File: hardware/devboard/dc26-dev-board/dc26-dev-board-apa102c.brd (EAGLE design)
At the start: 160 x 100 mm, 84 parts, among them CN1 JST, IC1 STM32F411RET6, M10 STM32-Breakout-2, P1 SSSS811101, U1 ESP-WROOM-32, Y1 ABL-8.000MHZ-B2

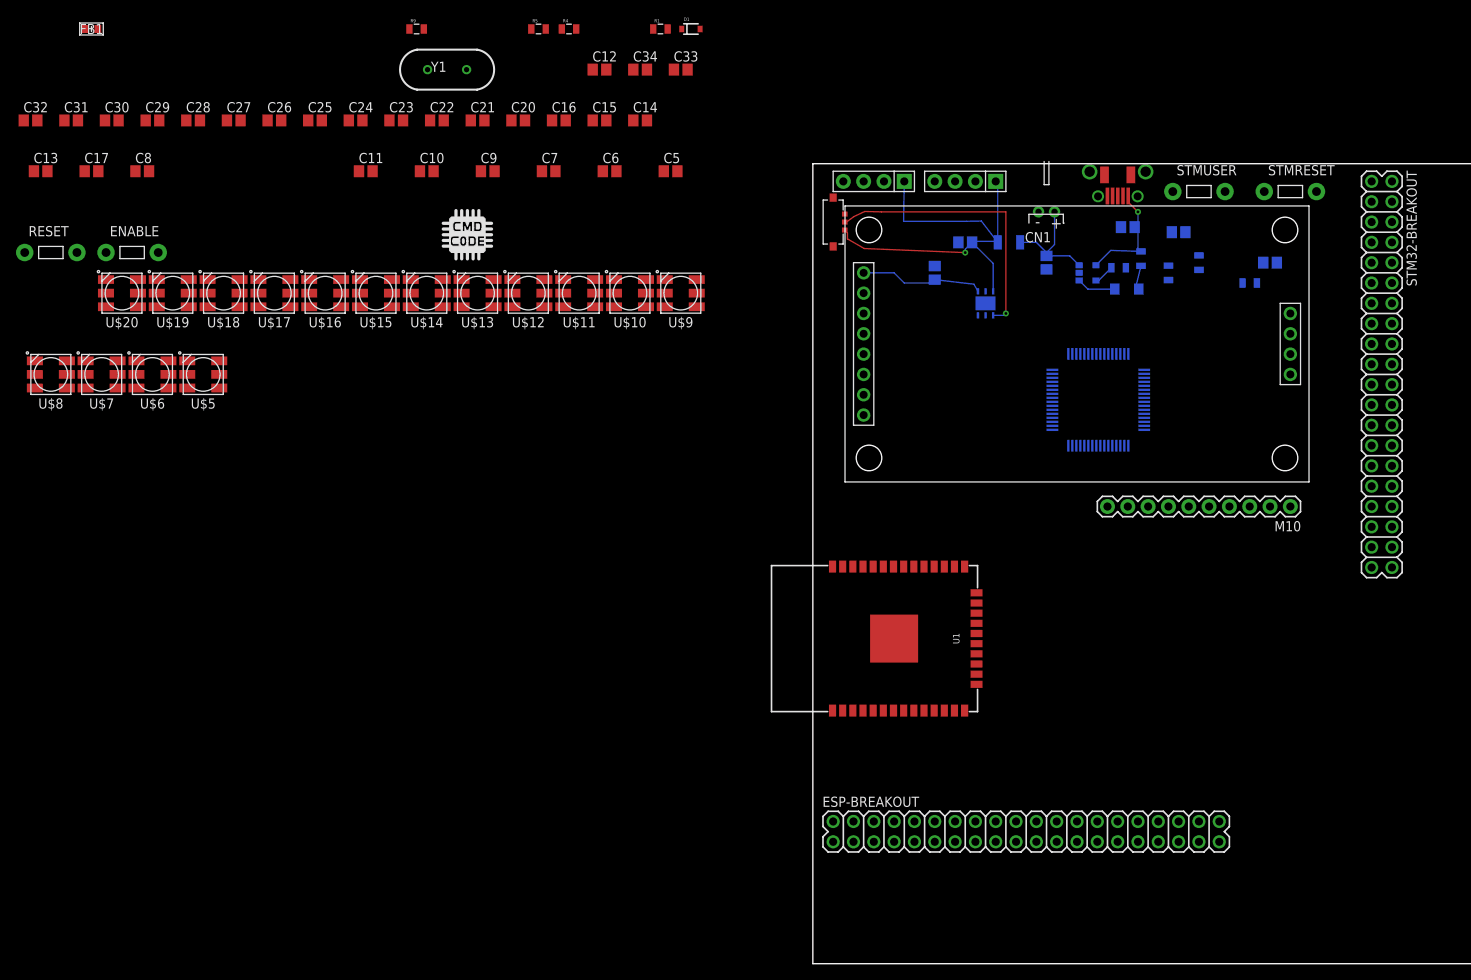
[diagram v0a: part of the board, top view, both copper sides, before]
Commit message: power run not but not gpio
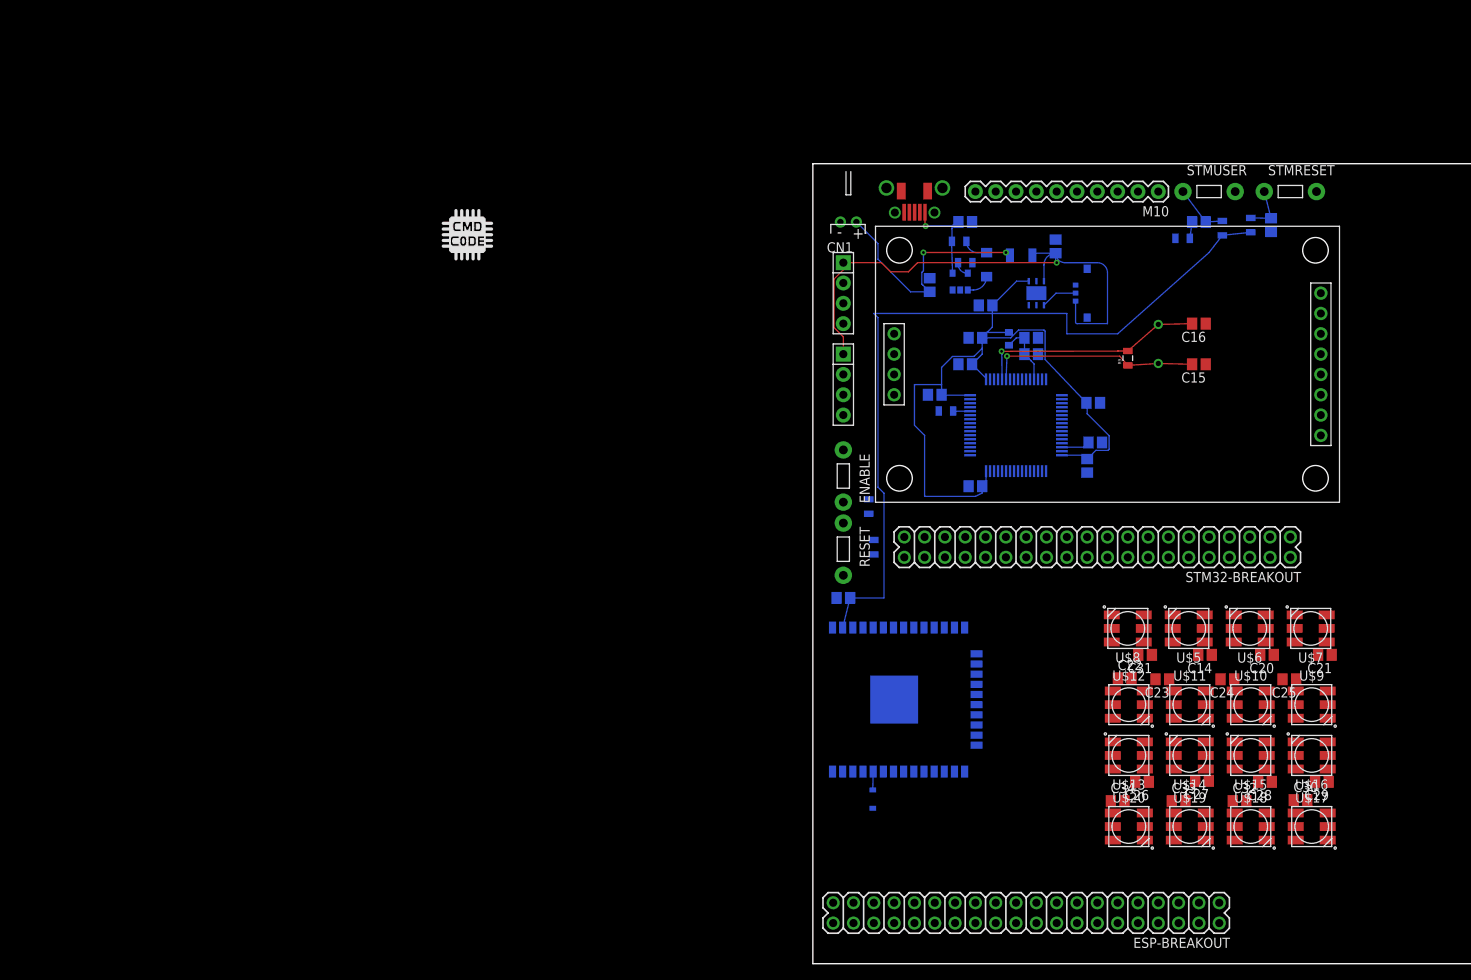
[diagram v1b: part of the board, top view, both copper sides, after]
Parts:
- moved C32 173.4 mm to (53.3, 20.3)
- moved C30 171.2 mm to (61.0, 20.4)
- moved C29 167.9 mm to (63.6, 22.7), turned to 180 degrees
- moved C28 157.4 mm to (56.5, 22.7), turned to 180 degrees
- moved U$7 154.4 mm to (62.2, 41.9)
- moved C31 149.9 mm to (41.5, 38.6), turned to 180 degrees
- moved C27 146.5 mm to (48.6, 22.9), turned to 180 degrees
- moved U$17 145.8 mm to (62.4, 17.1), turned to 180 degrees
- moved U$18 144.7 mm to (54.7, 17.1), turned to 180 degrees
- moved U$19 143.6 mm to (47.1, 17.1), turned to 180 degrees
- moved U$20 142.4 mm to (39.5, 17.1), turned to 180 degrees
- moved U$6 140.8 mm to (54.6, 41.9)
- moved C25 140.4 mm to (59.6, 35.6), turned to 180 degrees
- moved U$8 138.3 mm to (39.4, 41.9)
- moved C26 136.4 mm to (41.1, 22.7), turned to 180 degrees
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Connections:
- net VCC4: now also U$7.1
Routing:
- net VCC: track 15.6 -> 191.8 mm
- net VIN-EN: track 34.9 -> 4.57 mm, vias 1 -> 0
- net OSC_IN: track 0.00 -> 29.1 mm, vias 0 -> 1
- net OSC_OUT: track 0.00 -> 26.6 mm, vias 0 -> 1
- net VCC1: track 13.9 -> 30.3 mm, vias 0 -> 2
- net VIN: track 54.1 -> 68.9 mm
- net VDDA: track 0.00 -> 8.01 mm
- net PC13: track 0.00 -> 6.83 mm
- net NRST: track 0.00 -> 5.99 mm
- net N$20: track 0.00 -> 3.56 mm
- net ESP-RX0: track 0.00 -> 2.30 mm
- net BOOT0: track 0.00 -> 2.14 mm
- net N$4: track 0.00 -> 2.05 mm
- net N$3: track 4.90 -> 3.04 mm
- net VCC0: track 14.0 -> 12.8 mm
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
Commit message: after chatting with bunni
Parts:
- moved C15 6.48 mm to (41.9, 73.7), turned to 90 degrees
- moved C16 6.48 mm to (41.9, 78.7), turned to 270 degrees
- moved Y1 4.32 mm to (47.0, 75.4)
- moved C3 1.27 mm to (30.4, 90.9)
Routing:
- net VCC: track 191.8 -> 199.0 mm, vias 0 -> 1
- net VCC1: track 30.3 -> 33.0 mm
- net VIN: track 68.9 -> 71.1 mm, vias 1 -> 2
- net OSC_IN: track 29.1 -> 28.0 mm

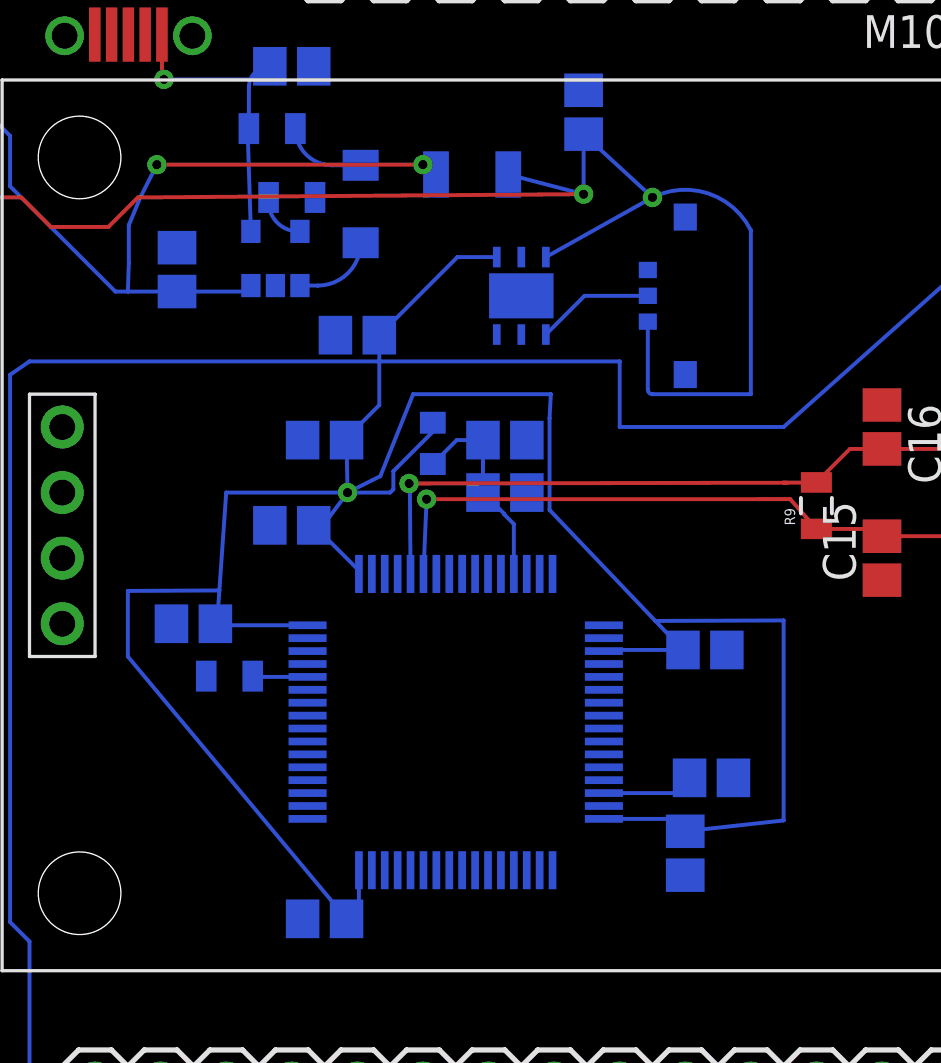
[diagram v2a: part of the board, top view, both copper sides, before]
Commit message: fixed all board errors except air wires
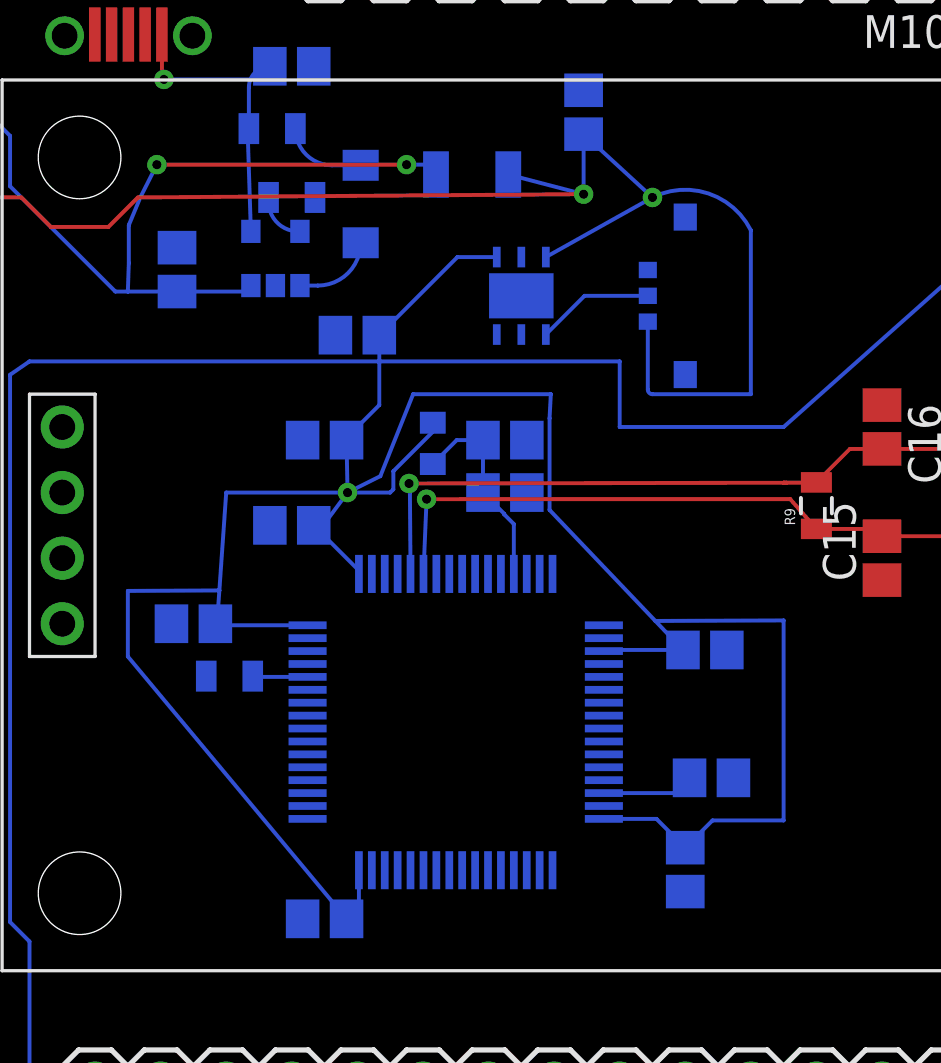
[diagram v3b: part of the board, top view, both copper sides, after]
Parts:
- moved C7 0.63 mm to (34.3, 61.6)
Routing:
- net VCC: track 199.0 -> 199.6 mm
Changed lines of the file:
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@@
 <element name="C5" library="dc-26" package="C0805" value="100nF" x="20.32" y="59.69" rot="MR0"/>
 <element name="C6" library="dc-26" package="C0805" value="100nF" x="35.052" y="70.104" rot="MR180"/>
-<element name="C7" library="dc-26" package="C0805" value="100nF" x="34.29" y="62.23" rot="MR270"/>
+<element name="C7" library="dc-26" package="C0805" value="100nF" x="34.29" y="61.595" rot="MR270"/>
 <element name="C8" library="dc-26" package="C0805" value="4.7uF" x="20.32" y="78.232" rot="MR0"/>
 <element name="C9" library="dc-26" package="C0805" value="100nF" x="15.24" y="71.12" rot="MR0"/>
@@
 <wire x1="28.155" y1="78.232" x2="42.838" y2="35.56" width="0" layer="19" extent="1-1"/>
 <wire x1="57.277" y1="91.479" x2="58.713" y2="35.56" width="0" layer="19" extent="1-1"/>
-<wire x1="34.29" y1="61.38" x2="41.91" y2="72.81" width="0" layer="19" extent="1-1"/>
+<wire x1="34.29" y1="60.745" x2="41.91" y2="72.81" width="0" layer="19" extent="1-1"/>
 <wire x1="3.81" y1="80.01" x2="18.415" y2="84.217" width="0" layer="19" extent="1-1"/>
 <wire x1="22.86" y1="96.52" x2="35.902" y2="70.104" width="0" layer="19" extent="1-1"/>
@@
 <wire x1="13.1892" y1="87.6444875" x2="13.8242" y2="88.9" width="0.1524" layer="16"/>
 <wire x1="12.7374" y1="86.5576875" x2="13.1892" y2="87.6444875" width="0.1524" layer="16"/>
-<wire x1="13.8242" y1="88.9" x2="24.13" y2="88.9" width="0.1524" layer="1"/>
-<via x="24.13" y="88.9" extent="1-16" drill="0.35"/>
-<wire x1="24.13" y1="88.9" x2="24.254" y2="88.9" width="0.1524" layer="16"/>
+<wire x1="13.8242" y1="88.9" x2="23.495" y2="88.9" width="0.1524" layer="1"/>
+<via x="23.495" y="88.9" extent="1-16" drill="0.35"/>
+<wire x1="23.495" y1="88.9" x2="24.254" y2="88.9" width="0.1524" layer="16"/>
 <wire x1="24.254" y1="88.9" x2="24.635" y2="88.519" width="0.1524" layer="16"/>
 <wire x1="14.605" y1="83.986" x2="17.234" y2="83.986" width="0.1524" layer="16"/>
@@
 <wire x1="29.0336" y1="79.0766875" x2="29.0336" y2="75.5264" width="0.1524" layer="16"/>
 <wire x1="34.202" y1="70.104" x2="34.29" y2="70.016" width="0.1524" layer="16"/>
-<wire x1="34.29" y1="63.08" x2="33.81" y2="63.56" width="0.1524" layer="16"/>
-<wire x1="33.81" y1="63.56" x2="31.138" y2="63.56" width="0.1524" layer="16"/>
 <wire x1="16.09" y1="71.12" x2="16.15" y2="71.06" width="0.1524" layer="16"/>
 <wire x1="16.15" y1="71.06" x2="19.662" y2="71.06" width="0.1524" layer="16"/>
@@
 <wire x1="33.131915625" y1="71.226671875" x2="38.1" y2="71.247" width="0.1524" layer="16"/>
 <wire x1="38.1" y1="71.247" x2="38.1" y2="63.5" width="0.1524" layer="16"/>
-<wire x1="38.1" y1="63.5" x2="34.29" y2="63.08" width="0.1524" layer="16"/>
 <wire x1="16.244453125" y1="72.4086" x2="12.7" y2="72.39" width="0.1524" layer="16"/>
 <wire x1="12.7" y1="72.39" x2="12.7" y2="69.85" width="0.1524" layer="16"/>
 <wire x1="12.7" y1="69.85" x2="21.17" y2="59.69" width="0.1524" layer="16"/>
+<wire x1="31.138" y1="63.56" x2="33.175" y2="63.56" width="0.1524" layer="16"/>
+<wire x1="33.175" y1="63.56" x2="34.29" y2="62.445" width="0.1524" layer="16"/>
+<wire x1="38.1" y1="63.5" x2="35.345" y2="63.5" width="0.1524" layer="16"/>
+<wire x1="35.345" y1="63.5" x2="34.29" y2="62.445" width="0.1524" layer="16"/>
 <wire x1="59.69" y1="53.34" x2="63.5" y2="66.04" width="0" layer="19" extent="1-1"/>
 <wire x1="38.1" y1="63.5" x2="59.69" y2="53.34" width="0" layer="19" extent="16-16"/>

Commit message: ran power to apa102
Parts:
- moved M10 22.9 mm to (20.3, 96.5), turned to 0 degrees
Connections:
- removed net GPIO_APA102_DATA: STM32-BREAKOUT.16
- removed net PC9: STM32-BREAKOUT.18
- removed net VCC10: C27.1
- removed net VCC11: C28.1
- removed net VCC12: C29.1
- removed net VCC13: C30.1
- removed net VCC14: C32.1
- removed net VCC15: C33.1
- removed net VCC16: C34.1
- removed net VCC2: C14.1
- removed net VCC3: C20.1
- removed net VCC4: C21.1, U$7.1
- removed net VCC5: C22.1
- removed net VCC6: C23.1
- removed net VCC7: C24.1
- removed net VCC8: C25.1
- removed net VCC9: C26.1
- net APA102_CLK: now also STM32-BREAKOUT.18
- net APA102_DATA: now also STM32-BREAKOUT.16, U$8.4
- net VCC1: no longer C31.1
- net VIN: now also C14.1, C20.1, C21.1, C22.1, C23.1, C24.1, C25.1, C26.1, C27.1, C28.1, C29.1, C30.1, C31.1, C32.1, C33.1, C34.1, U$10.1, U$11.1, U$12.1, U$13.1, U$14.1, U$15.1, U$16.1, U$17.1, U$18.1, U$19.1, U$20.1, U$5.1, U$6.1, U$7.1, U$8.1, U$9.1
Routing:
- net VIN: track 71.1 -> 281.1 mm
- net VCC: track 199.6 -> 281.2 mm, vias 1 -> 3

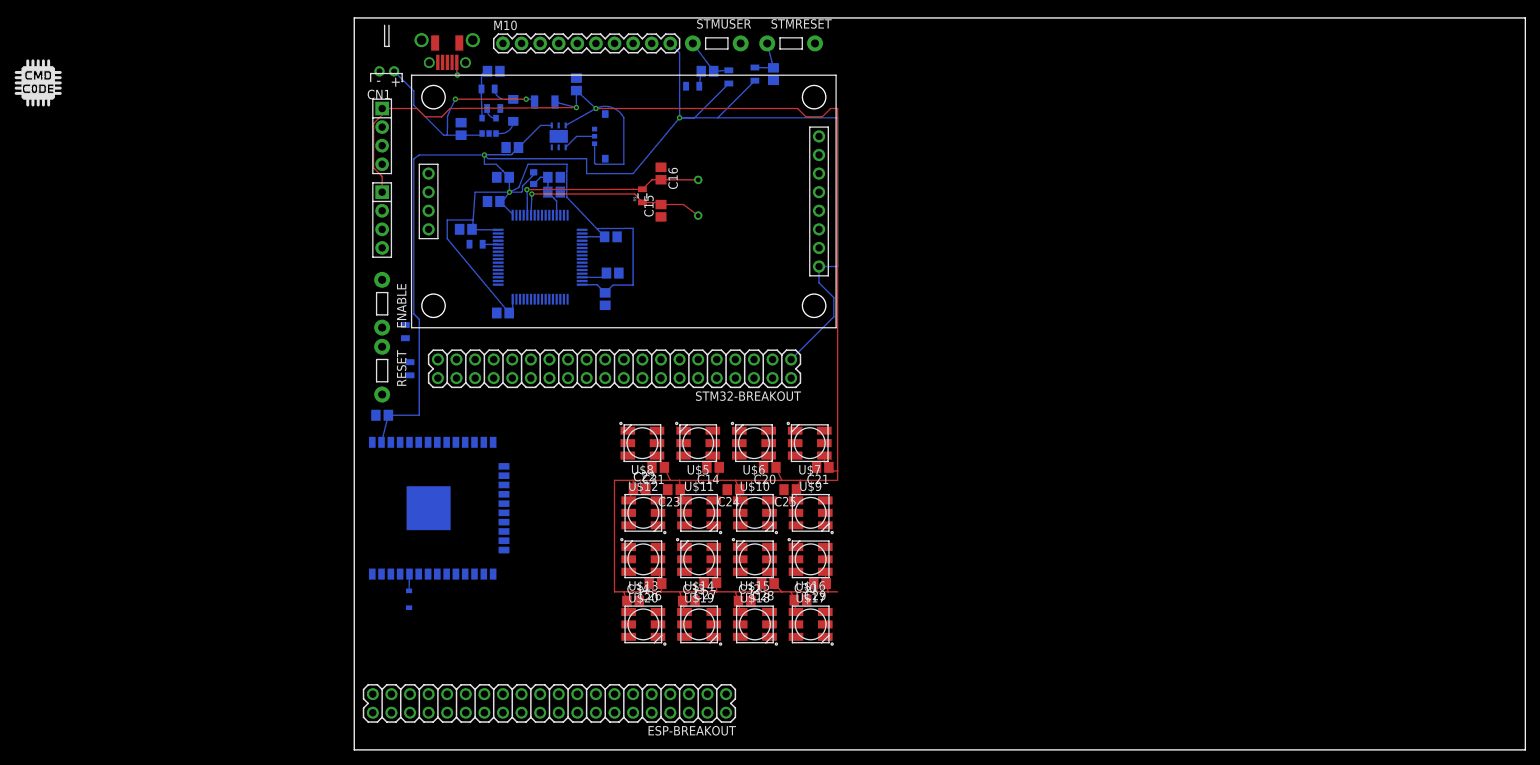
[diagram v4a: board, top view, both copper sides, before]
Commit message: fixed an overlap moved logos onto board
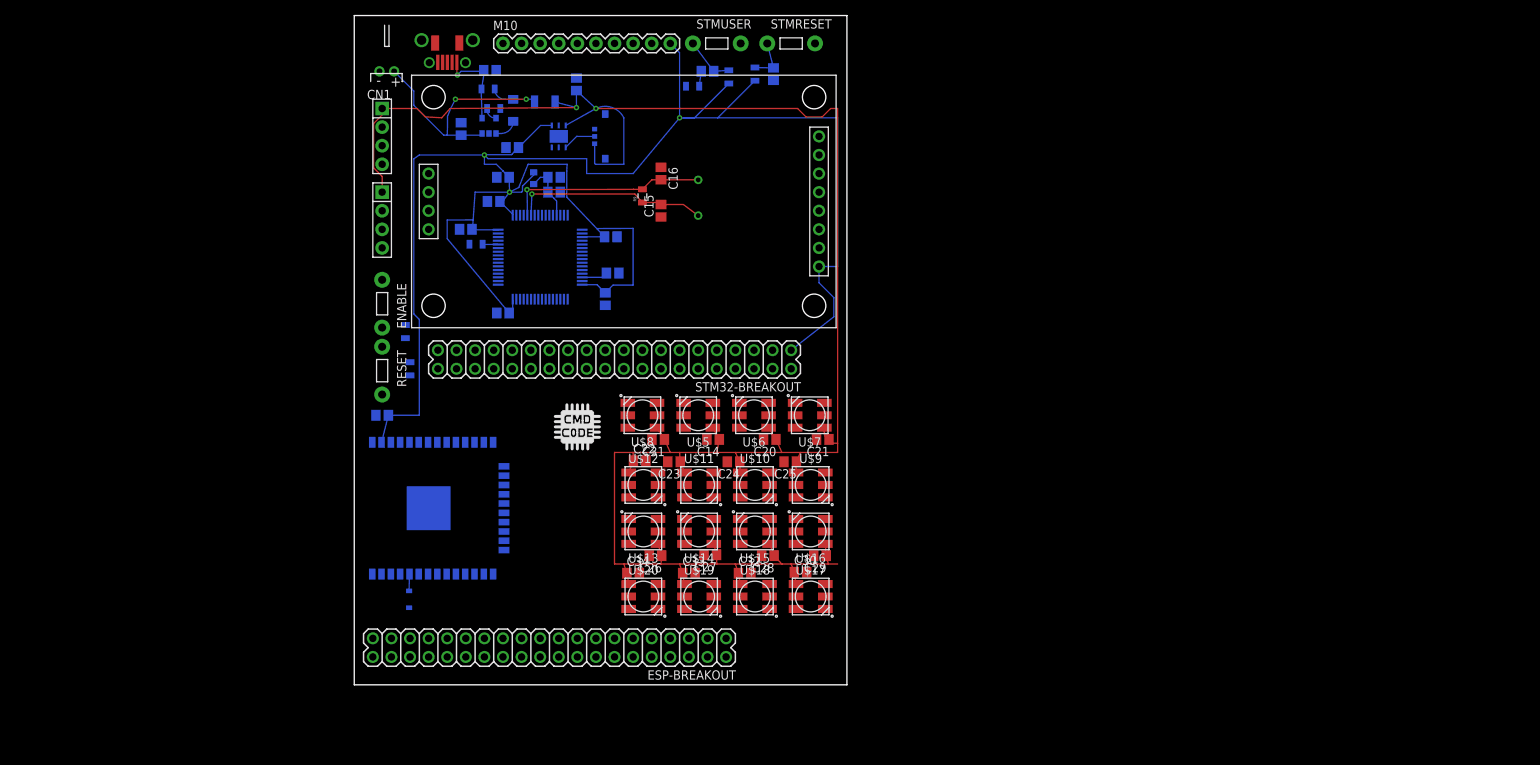
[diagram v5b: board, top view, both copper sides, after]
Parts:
- moved U$3 165.4 mm to (61.0, 12.7)
- moved U$4 164.3 mm to (54.6, 12.7)
- moved U$2 87.4 mm to (30.5, 44.5)
- moved ESP-BREAKOUT 7.62 mm to (26.7, 14.0)
- moved C14 3.81 mm to (49.0, 42.4)
- moved C20 3.81 mm to (56.8, 42.4)
- moved C21 3.81 mm to (64.0, 42.4)
- moved C22 3.81 mm to (39.0, 39.5)
- moved C27 3.81 mm to (48.6, 26.7)
- moved C30 3.81 mm to (61.0, 24.3)
- moved C31 3.81 mm to (41.5, 42.4)
- moved U$10 3.81 mm to (54.7, 36.2)
- moved U$11 3.81 mm to (47.1, 36.2)
- moved U$12 3.81 mm to (39.5, 36.2)
- moved U$5 3.81 mm to (47.0, 45.7)
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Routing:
- net VIN: track 281.1 -> 277.4 mm
- net VCC: track 281.2 -> 280.4 mm
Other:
- board size 160 x 100 mm -> 67.3 x 91.4 mm

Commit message: board sent to oshpark
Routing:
- net GND: track 0.00 -> 721.8 mm, vias 0 -> 10
- net ESP_CS: track 0.00 -> 145.8 mm, vias 0 -> 2
- net SPI3_ESP_MOSI: track 0.00 -> 122.7 mm, vias 0 -> 4
- net SPI2_LCD_SCK: track 0.00 -> 120.1 mm, vias 0 -> 3
- net SPI3_ESP_MISO: track 0.00 -> 116.8 mm, vias 0 -> 6
- net LCD_BACKLIGHT: track 0.00 -> 114.3 mm, vias 0 -> 4
- net PC13: track 6.83 -> 118.2 mm, vias 0 -> 3
- net SPI3_ESP_SCK: track 0.00 -> 104.9 mm, vias 0 -> 4
- net LCD_DATA_CMD: track 0.00 -> 101.4 mm, vias 0 -> 2
- net LCD_RESET: track 0.00 -> 95.8 mm, vias 0 -> 4
- net NRST: track 5.99 -> 81.6 mm, vias 0 -> 4
- net PC14: track 0.00 -> 74.2 mm, vias 0 -> 5
- net SENSOR_VN: track 0.00 -> 72.1 mm, vias 0 -> 1
- net IO35: track 0.00 -> 70.7 mm, vias 0 -> 1
- net ESP-TX0: track 0.00 -> 70.2 mm
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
